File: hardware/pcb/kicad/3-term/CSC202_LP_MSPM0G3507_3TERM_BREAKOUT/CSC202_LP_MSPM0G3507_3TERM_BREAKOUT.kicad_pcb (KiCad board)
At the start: 2 copper layers, 90 x 35 mm, 10 parts, among them J1 J_IN1/J_IN3, J2 J_IN4/J_IN2, J3 J_OUT1, J4 J_OUT3, J5 J_OUT4, J6 J_OUT2

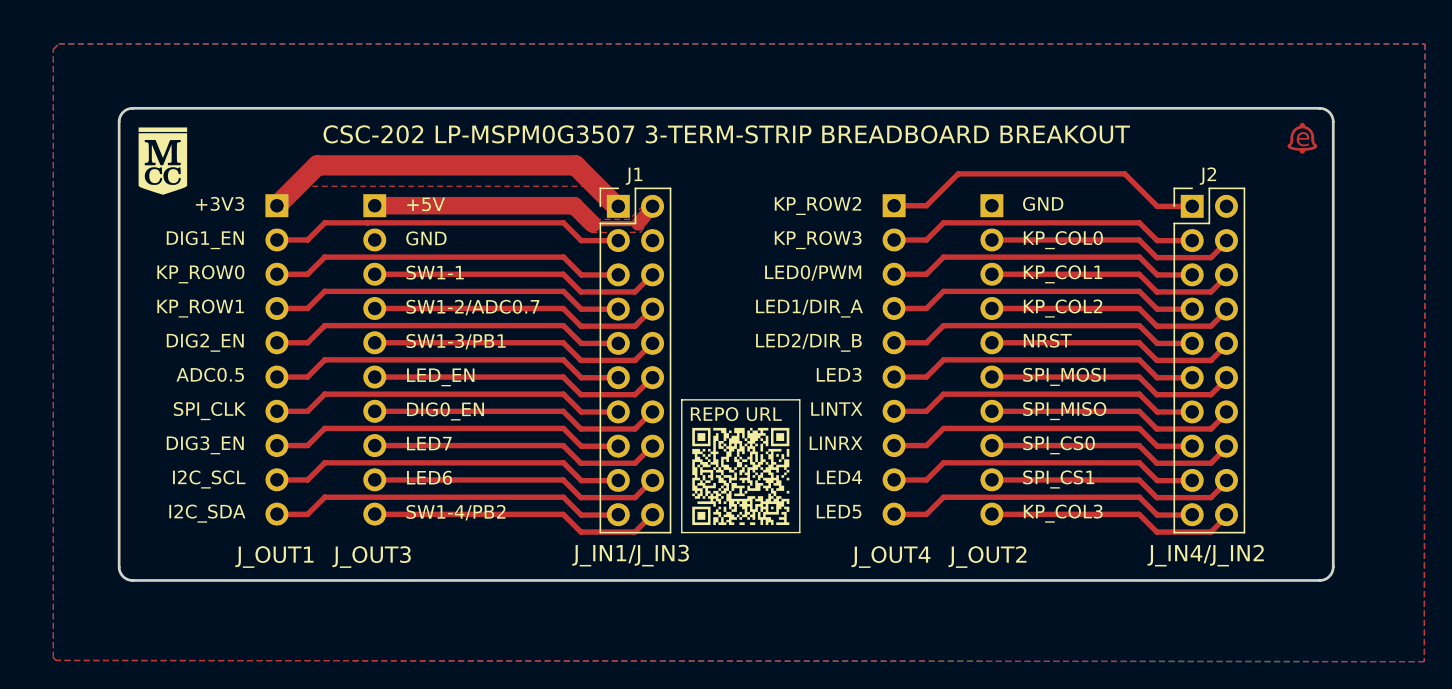
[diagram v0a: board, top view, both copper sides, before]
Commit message: implemented kibot and mkdocs
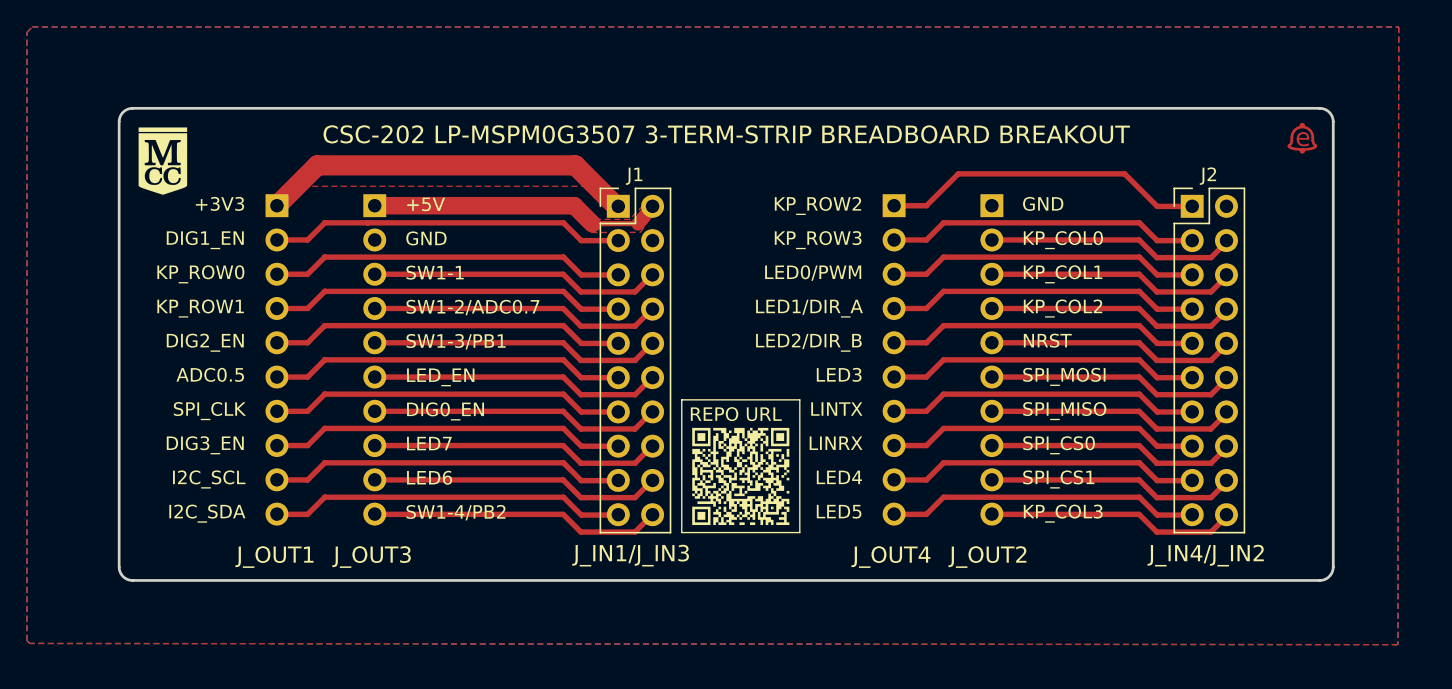
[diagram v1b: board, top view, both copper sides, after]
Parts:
- renumbered LOGO** to LOGO2
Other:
- board text added: "LP-MSPM0G3507"

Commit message: init led module
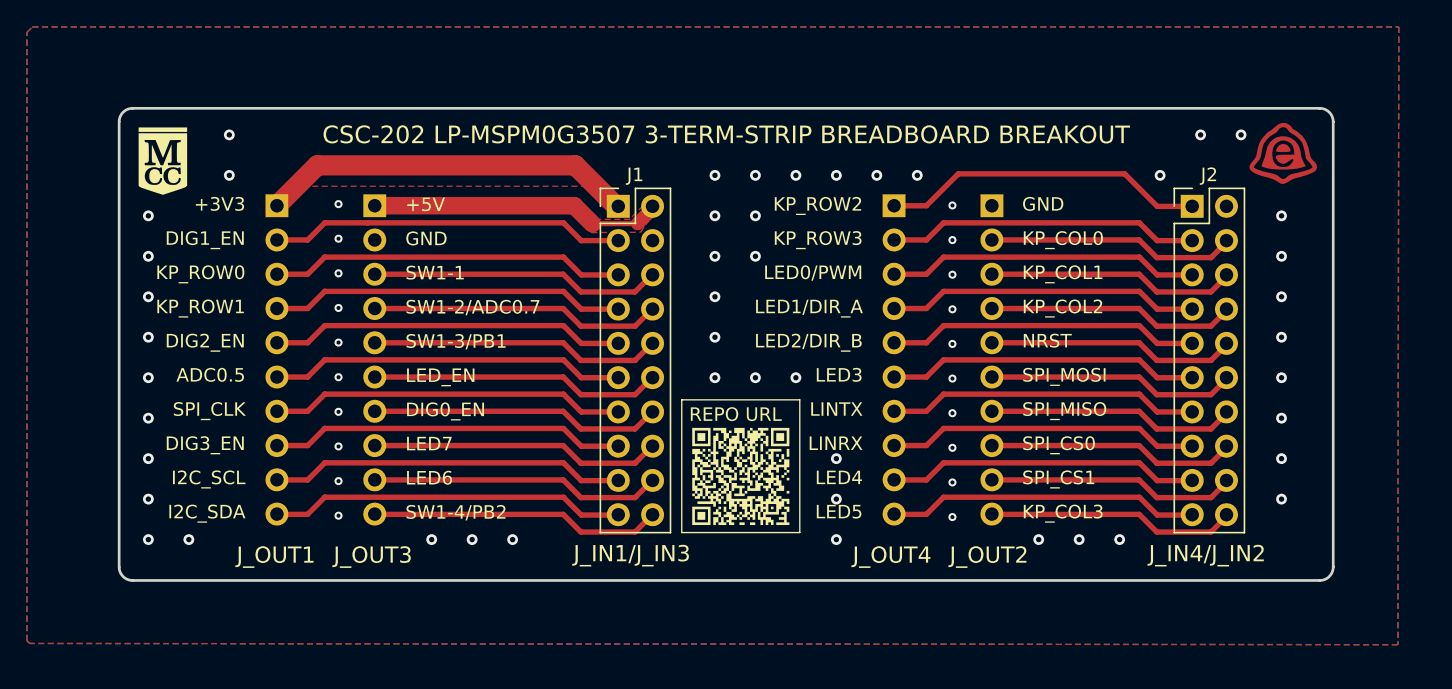
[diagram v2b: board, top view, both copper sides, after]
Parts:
- removed LOGO2: Logo, 01-Shared_Project_Footprints:Makers-Mark_Eli_Bell
- added G***: LOGO, 3-term:Eli_Bell_Logo, F.Cu at (175.4, 83.3)
- G1, G2: footprint 01-Shared_Project_Footprints:Repo_URL_QR -> 3-term:Repo_URL_QR
- J1: footprint 01-Shared_Project_Footprints:PinHeader_2x10_P2.54mm_Vertical_J1-J3 -> 3-term:PinHeader_2x10_P2.54mm_Vertical_J1-J3
- J2: footprint 01-Shared_Project_Footprints:PinHeader_2x10_P2.54mm_Vertical_J2-J4 -> 3-term:PinHeader_2x10_P2.54mm_Vertical_J2-J4
- J3, J4, J5, J6: footprint Connector_PinHeader_2.54mm:PinHeader_1x10_P2.54mm_Vertical -> 3-term:PinHeader_1x10_P2.54mm_Vertical
- LOGO1: footprint 01-Shared_Project_Footprints:MCC-Logo -> 3-term:MCC-Logo
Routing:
- net +5V: track 20.6 -> 21.8 mm
- net GND: vias 0 -> 67
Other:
- board text added: "{ "ViaStitching": "0.2", "stitch_zone_0": { "HSpacing": "1", "VSpacing": "1", "HOffset": "0", "VOffset": "0", "Clearance": "0", "Randomize": false } }"
- board text added: "{ "ViaStitching": "0.2", "stitch_zone_0": { "HSpacing": "3", "VSpacing": "3", "HOffset": "0", "VOffset": "-1.5", "Clearance": ".2", "Randomize": false } }"
- board text added: "{ "ViaStitching": "0.2", "stitch_zone_0": { "HSpacing": "3", "VSpacing": "3", "HOffset": "0", "VOffset": "0", "Clearance": ".2", "Randomize": false } }"
- board text added: "{ "ViaStitching": "0.2", "stitch_zone_0": { "HSpacing": "3", "VSpacing": "3", "HOffset": "0", "VOffset": "0", "Clearance": ".4", "Randomize": false } }"
- board text added: "{ "ViaStitching": "0.2", "stitch_zone_0": { "HSpacing": "3", "VSpacing": "3", "HOffset": "0", "VOffset": "0", "Clearance": ".5", "Randomize": false } }"
- board text added: "{ "ViaStitching": "0.2", "stitch_zone_0": { "HSpacing": "3", "VSpacing": "3", "HOffset": "0", "VOffset": "1.5", "Clearance": ".2", "Randomize": false } }"
- board text added: "{ "ViaStitching": "0.2", "stitch_zone_0": { "HSpacing": "3", "VSpacing": "3", "HOffset": "0", "VOffset": "2", "Clearance": ".25", "Randomize": false } }"
